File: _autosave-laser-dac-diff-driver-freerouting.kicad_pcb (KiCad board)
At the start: 2 copper layers, 70.5 x 51.4 mm, 55 parts, among them IC401 DCDC-CONV_TRACO_TMH-XXXX_Dual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, P101 CONN_2, P102 CONN_3X2, P103 CONN_6X2, U101 AD5689RARUZ, U102 74HC04, U201 OP470, U202 LM358, U401 LM317EMP, U402 LM317EMP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

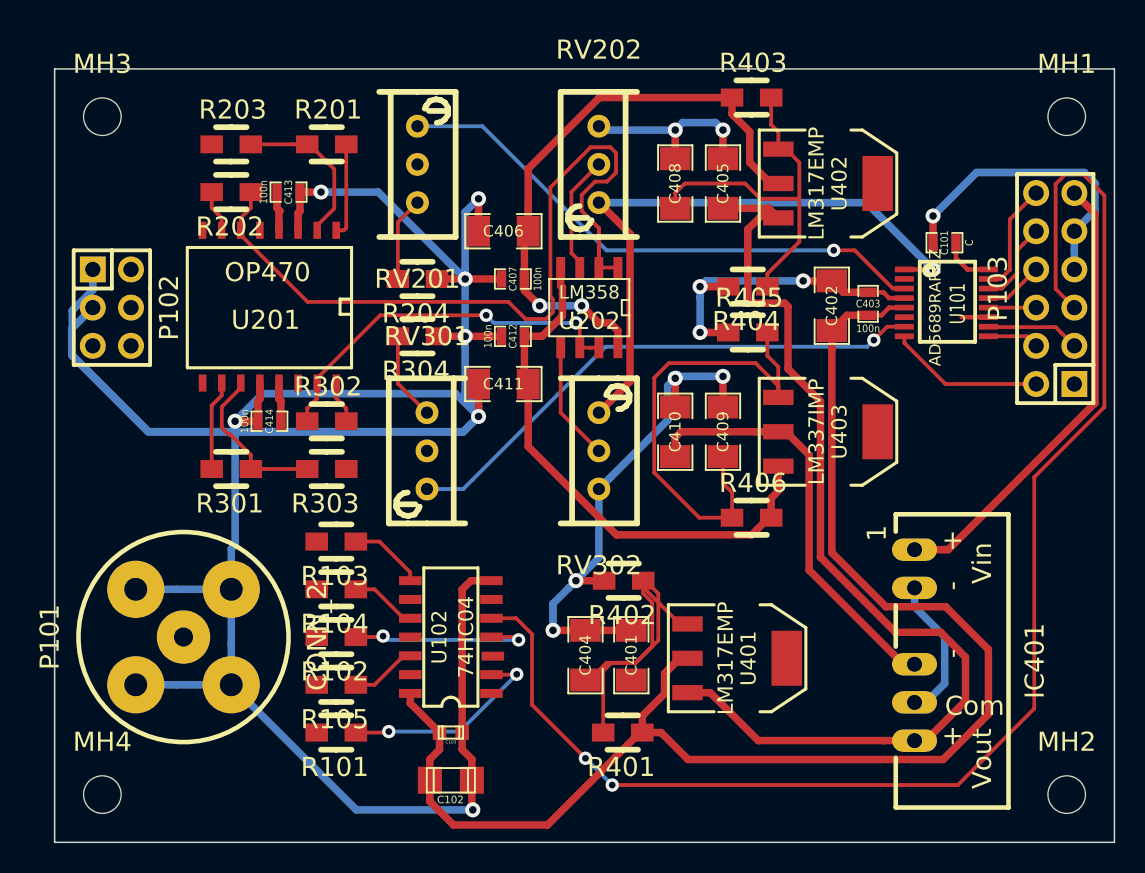
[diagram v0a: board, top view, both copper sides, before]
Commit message: A few autorouter attempts and a new board layout (component positions). Removed voltage selector for MOD driver, 5V only now.
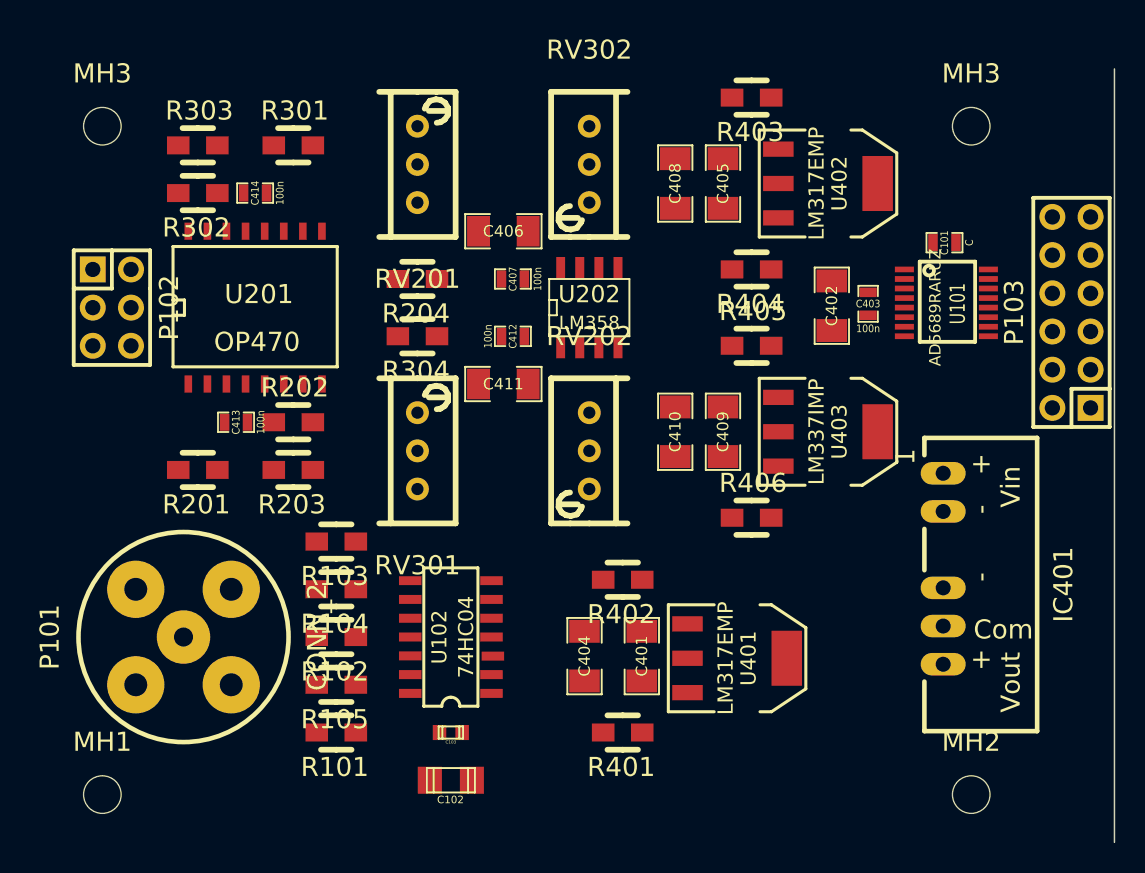
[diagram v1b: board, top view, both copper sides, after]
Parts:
- moved R201 23.3 mm to (208.3, 61.0), turned to 180 degrees
- moved R303 23.2 mm to (208.3, 39.4), turned to 0 degrees
- moved R203 22.0 mm to (214.6, 61.0), turned to 180 degrees
- moved R301 21.9 mm to (214.6, 39.4), turned to 0 degrees
- moved RV202 19.1 mm to (234.3, 59.7)
- moved RV302 19.1 mm to (234.3, 40.6), turned to 0 degrees
- moved R302 17.4 mm to (208.3, 42.5), turned to 180 degrees
- moved R202 15.9 mm to (214.6, 57.8), turned to 0 degrees
- moved C413 15.7 mm to (210.8, 57.8), turned to 180 degrees
- moved C414 15.2 mm to (212.1, 42.5), turned to 180 degrees
- moved MH3 6.38 mm to (259.7, 38.1)
- moved MH2 6.35 mm to (259.7, 82.5)
- moved IC401 5.43 mm to (260.4, 68.6)
- moved P103 1.92 mm to (266.4, 50.5)
- moved R404 1.17 mm to (245.1, 47.6)
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- renumbered MH4 to MH1, MH1 to MH3
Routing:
- net DGND: track 300.9 -> 0.00 mm, vias 17 -> 0
- net +5VD: track 96.1 -> 0.00 mm
- net /MOD_IN: track 94.4 -> 0.00 mm, vias 2 -> 0
- net /powersupply/+Vout_unreg: track 67.3 -> 0.00 mm
- net Net-(R202-Pad1): track 53.8 -> 0.00 mm
- net VAA: track 42.1 -> 0.00 mm, vias 2 -> 0
- net /analog/+Vref: track 41.7 -> 0.00 mm, vias 1 -> 0
- net -VAA: track 39.1 -> 0.00 mm
- net /analog/In1: track 36.9 -> 0.00 mm, vias 1 -> 0
- net /analog2/In1: track 36.2 -> 0.00 mm, vias 1 -> 0
- net Net-(C409-Pad2): track 31.7 -> 0.00 mm
- net /powersupply/+Vin: track 30.6 -> 0.00 mm
- net /powersupply/-Vout_unreg: track 28.7 -> 0.00 mm
- net Net-(C404-Pad1): track 27.5 -> 0.00 mm
- net Net-(R302-Pad1): track 25.3 -> 0.00 mm, vias 2 -> 0
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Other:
- board outline removed
